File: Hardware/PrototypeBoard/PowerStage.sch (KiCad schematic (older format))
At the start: 20 parts, among them Q1 Q_NMOS_SGD, Q2 Q_NMOS_SGD, Q3 Q_NMOS_SGD, Q4 Q_NMOS_SGD, Q5 Q_NMOS_SGD, Q6 Q_NMOS_SGD

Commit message: some more layout work
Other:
- moved on the sheet: C5, C7
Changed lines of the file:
@@
 L CP C5
 U 1 1 5B00A755
-P 2900 6150
-F 0 "C5" H 2925 6250 50  0000 L CNN
-F 1 "220μF, 50V" H 2925 6050 50  0000 L CNN
-F 2 "Capacitors_SMD:CP_Elec_10x10" H 2938 6000 50  0001 C CNN
-F 3 "" H 2900 6150 50  0001 C CNN
-	1    2900 6150
+P 1500 4950
+F 0 "C5" H 1525 5050 50  0000 L CNN
+F 1 "220μF, 50V" H 1525 4850 50  0000 L CNN
+F 2 "Capacitors_SMD:CP_Elec_10x10" H 1538 4800 50  0001 C CNN
+F 3 "" H 1500 4950 50  0001 C CNN
+	1    1500 4950
 	1    0    0    -1
 $EndComp
@@
 L CP C7
 U 1 1 5B00A808
-P 3300 6150
-F 0 "C7" H 3325 6250 50  0000 L CNN
-F 1 "220μF, 50V" H 3325 6050 50  0000 L CNN
-F 2 "Capacitors_SMD:CP_Elec_10x10" H 3338 6000 50  0001 C CNN
-F 3 "" H 3300 6150 50  0001 C CNN
-	1    3300 6150
+P 1900 4950
+F 0 "C7" H 1925 5050 50  0000 L CNN
+F 1 "220μF, 50V" H 1925 4850 50  0000 L CNN
+F 2 "Capacitors_SMD:CP_Elec_10x10" H 1938 4800 50  0001 C CNN
+F 3 "" H 1900 4950 50  0001 C CNN
+	1    1900 4950
 	1    0    0    -1
 $EndComp
@@
 L GNDPWR #PWR021
 U 1 1 5B00BBB6
-P 3100 6500
-F 0 "#PWR021" H 3100 6300 50  0001 C CNN
-F 1 "GNDPWR" H 3100 6370 50  0000 C CNN
-F 2 "" H 3100 6450 50  0000 C CNN
-F 3 "" H 3100 6450 50  0000 C CNN
-	1    3100 6500
+P 1700 5300
+F 0 "#PWR021" H 1700 5100 50  0001 C CNN
+F 1 "GNDPWR" H 1700 5170 50  0000 C CNN
+F 2 "" H 1700 5250 50  0000 C CNN
+F 3 "" H 1700 5250 50  0000 C CNN
+	1    1700 5300
 	1    0    0    -1
 $EndComp
@@
 	7100 4700 7900 4700
 Wire Wire Line
-	2900 5900 3300 5900
-Wire Wire Line
-	2900 6400 3300 6400
+	1500 4700 1900 4700
+Wire Wire Line
+	1500 5200 1900 5200
 Wire Wire Line
 	2700 4800 2700 4700
@@
 	7900 5200 7900 5100
 Wire Wire Line
-	2900 6000 2900 5900
-Wire Wire Line
-	3300 5900 3300 6000
-Wire Wire Line
-	2900 6300 2900 6400
-Wire Wire Line
-	3300 6400 3300 6300
-Wire Wire Line
-	3100 6500 3100 6400
-Connection ~ 3100 6400
+	1500 4800 1500 4700
+Wire Wire Line
+	1900 4700 1900 4800
+Wire Wire Line
+	1500 5100 1500 5200
+Wire Wire Line
+	1900 5200 1900 5100
+Wire Wire Line
+	1700 5300 1700 5200
+Connection ~ 1700 5200
 $Comp
 L +BATT #PWR022
@@
 L +BATT #PWR025
 U 1 1 5B00C9A4
-P 3100 5800
-F 0 "#PWR025" H 3100 5650 50  0001 C CNN
-F 1 "+BATT" H 3100 5940 50  0000 C CNN
-F 2 "" H 3100 5800 50  0000 C CNN
-F 3 "" H 3100 5800 50  0000 C CNN
-	1    3100 5800
-	1    0    0    -1
-$EndComp
-Wire Wire Line
-	3100 5800 3100 5900
-Connection ~ 3100 5900
+P 1700 4600
+F 0 "#PWR025" H 1700 4450 50  0001 C CNN
+F 1 "+BATT" H 1700 4740 50  0000 C CNN
+F 2 "" H 1700 4600 50  0000 C CNN
+F 3 "" H 1700 4600 50  0000 C CNN
+	1    1700 4600
+	1    0    0    -1
+$EndComp
+Wire Wire Line
+	1700 4600 1700 4700
+Connection ~ 1700 4700
 $Comp
 L Q_NMOS_SGD Q1

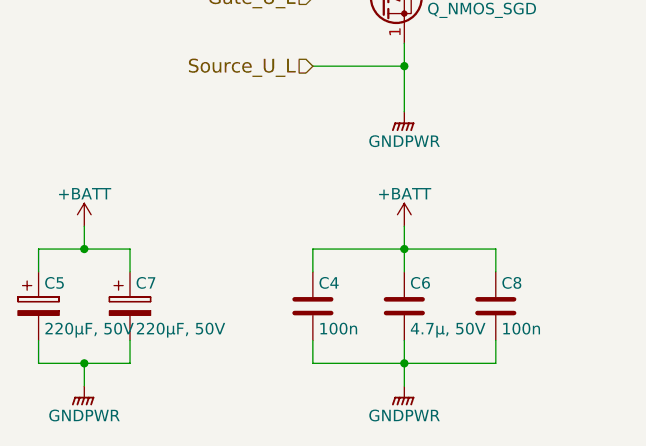
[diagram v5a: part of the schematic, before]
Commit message: assigned net classes and a few net names
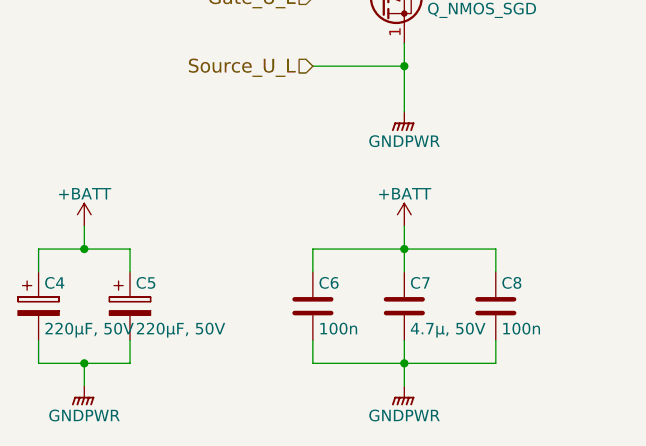
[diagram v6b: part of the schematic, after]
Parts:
- renumbered C5 to C4, C7 to C5, C4 to C6, C6 to C7
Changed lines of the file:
@@
 $EndComp
 $Comp
-L C C6
+L C C7
 U 1 1 5B00A350
 P 3100 4950
-F 0 "C6" H 3125 5050 50  0000 L CNN
+F 0 "C7" H 3125 5050 50  0000 L CNN
 F 1 "4.7μ, 50V" H 3125 4850 50  0000 L CNN
 F 2 "Capacitors_SMD:C_0805_HandSoldering" H 3138 4800 50  0001 C CNN
@@
 $EndComp
 $Comp
-L C C4
+L C C6
 U 1 1 5B00A488
 P 2700 4950
-F 0 "C4" H 2725 5050 50  0000 L CNN
+F 0 "C6" H 2725 5050 50  0000 L CNN
 F 1 "100n" H 2725 4850 50  0000 L CNN
 F 2 "Capacitors_SMD:C_0805_HandSoldering" H 2738 4800 50  0001 C CNN
@@
 $EndComp
 $Comp
-L CP C5
+L CP C4
 U 1 1 5B00A755
 P 1500 4950
-F 0 "C5" H 1525 5050 50  0000 L CNN
+F 0 "C4" H 1525 5050 50  0000 L CNN
 F 1 "220μF, 50V" H 1525 4850 50  0000 L CNN
 F 2 "Capacitors_SMD:CP_Elec_10x10" H 1538 4800 50  0001 C CNN
@@
 $EndComp
 $Comp
-L CP C7
+L CP C5
 U 1 1 5B00A808
 P 1900 4950
-F 0 "C7" H 1925 5050 50  0000 L CNN
+F 0 "C5" H 1925 5050 50  0000 L CNN
 F 1 "220μF, 50V" H 1925 4850 50  0000 L CNN
 F 2 "Capacitors_SMD:CP_Elec_10x10" H 1938 4800 50  0001 C CNN

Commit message: minor progress in layout
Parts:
- TP3, TP4, TP5: footprint Measurement_Points:Measurement_Point_Round-TH_Big -> Measurement_Points:Measurement_Point_Round-SMD-Pad_Small
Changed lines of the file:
@@
 F 0 "TP3" H 3100 3200 50  0000 C BNN
 F 1 "PhaseU" H 3100 3150 50  0000 C CNN
-F 2 "Measurement_Points:Measurement_Point_Round-TH_Big" H 3100 2900 50  0001 C CNN
+F 2 "Measurement_Points:Measurement_Point_Round-SMD-Pad_Small" H 3100 2900 50  0001 C CNN
 F 3 "" H 3100 2900 50  0001 C CNN
 	1    3100 2900
@@
 F 0 "TP4" H 5300 3200 50  0000 C BNN
 F 1 "PhaseV" H 5300 3150 50  0000 C CNN
-F 2 "Measurement_Points:Measurement_Point_Round-TH_Big" H 5300 2900 50  0001 C CNN
+F 2 "Measurement_Points:Measurement_Point_Round-SMD-Pad_Small" H 5300 2900 50  0001 C CNN
 F 3 "" H 5300 2900 50  0001 C CNN
 	1    5300 2900
@@
 F 0 "TP5" H 7500 3200 50  0000 C BNN
 F 1 "PhaseW" H 7500 3150 50  0000 C CNN
-F 2 "Measurement_Points:Measurement_Point_Round-TH_Big" H 7500 2900 50  0001 C CNN
+F 2 "Measurement_Points:Measurement_Point_Round-SMD-Pad_Small" H 7500 2900 50  0001 C CNN
 F 3 "" H 7500 2900 50  0001 C CNN
 	1    7500 2900

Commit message: more layout and some changes to schematic
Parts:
- TP3, TP4, TP5: footprint Measurement_Points:Measurement_Point_Round-SMD-Pad_Small -> Pin_Headers:Pin_Header_Straight_1x01_Pitch2.00mm
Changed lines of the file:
@@
 F 0 "TP3" H 3100 3200 50  0000 C BNN
 F 1 "PhaseU" H 3100 3150 50  0000 C CNN
-F 2 "Measurement_Points:Measurement_Point_Round-SMD-Pad_Small" H 3100 2900 50  0001 C CNN
+F 2 "Pin_Headers:Pin_Header_Straight_1x01_Pitch2.00mm" H 3100 2900 50  0001 C CNN
 F 3 "" H 3100 2900 50  0001 C CNN
 	1    3100 2900
@@
 F 0 "TP4" H 5300 3200 50  0000 C BNN
 F 1 "PhaseV" H 5300 3150 50  0000 C CNN
-F 2 "Measurement_Points:Measurement_Point_Round-SMD-Pad_Small" H 5300 2900 50  0001 C CNN
+F 2 "Pin_Headers:Pin_Header_Straight_1x01_Pitch2.00mm" H 5300 2900 50  0001 C CNN
 F 3 "" H 5300 2900 50  0001 C CNN
 	1    5300 2900
@@
 F 0 "TP5" H 7500 3200 50  0000 C BNN
 F 1 "PhaseW" H 7500 3150 50  0000 C CNN
-F 2 "Measurement_Points:Measurement_Point_Round-SMD-Pad_Small" H 7500 2900 50  0001 C CNN
+F 2 "Pin_Headers:Pin_Header_Straight_1x01_Pitch2.00mm" H 7500 2900 50  0001 C CNN
 F 3 "" H 7500 2900 50  0001 C CNN
 	1    7500 2900
